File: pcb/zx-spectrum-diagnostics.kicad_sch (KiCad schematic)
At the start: 13 parts, among them J101 Conn_01x04, U101 Pico, U102 Pico

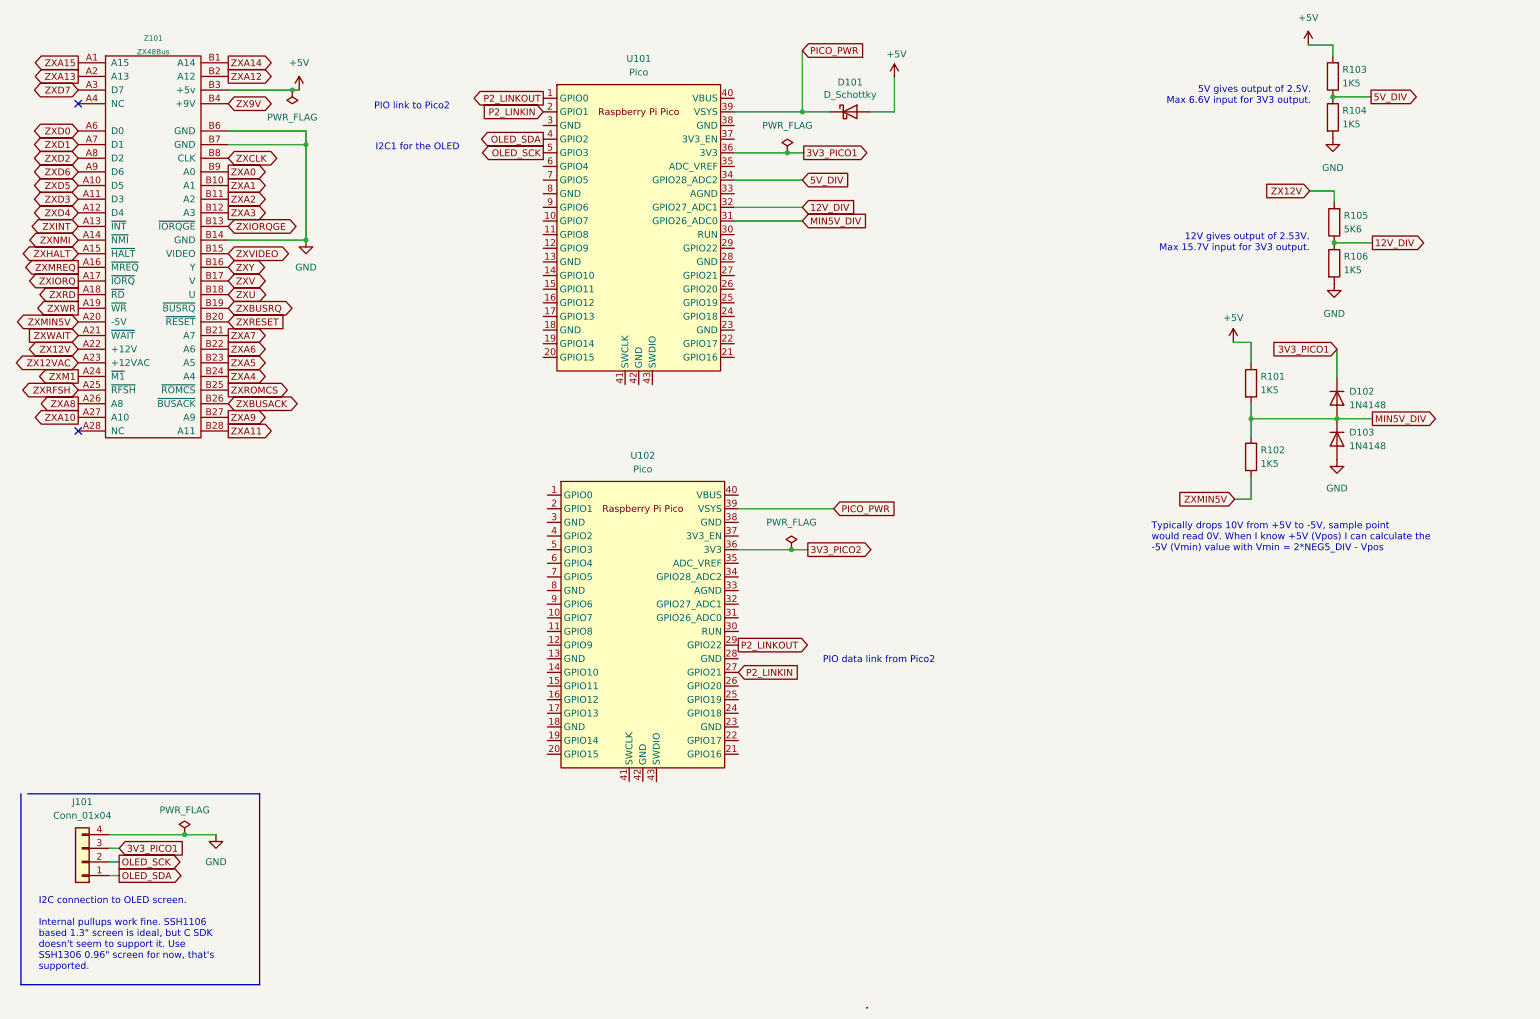
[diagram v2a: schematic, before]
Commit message: back out previous layout, rearrange connections to match edge connector
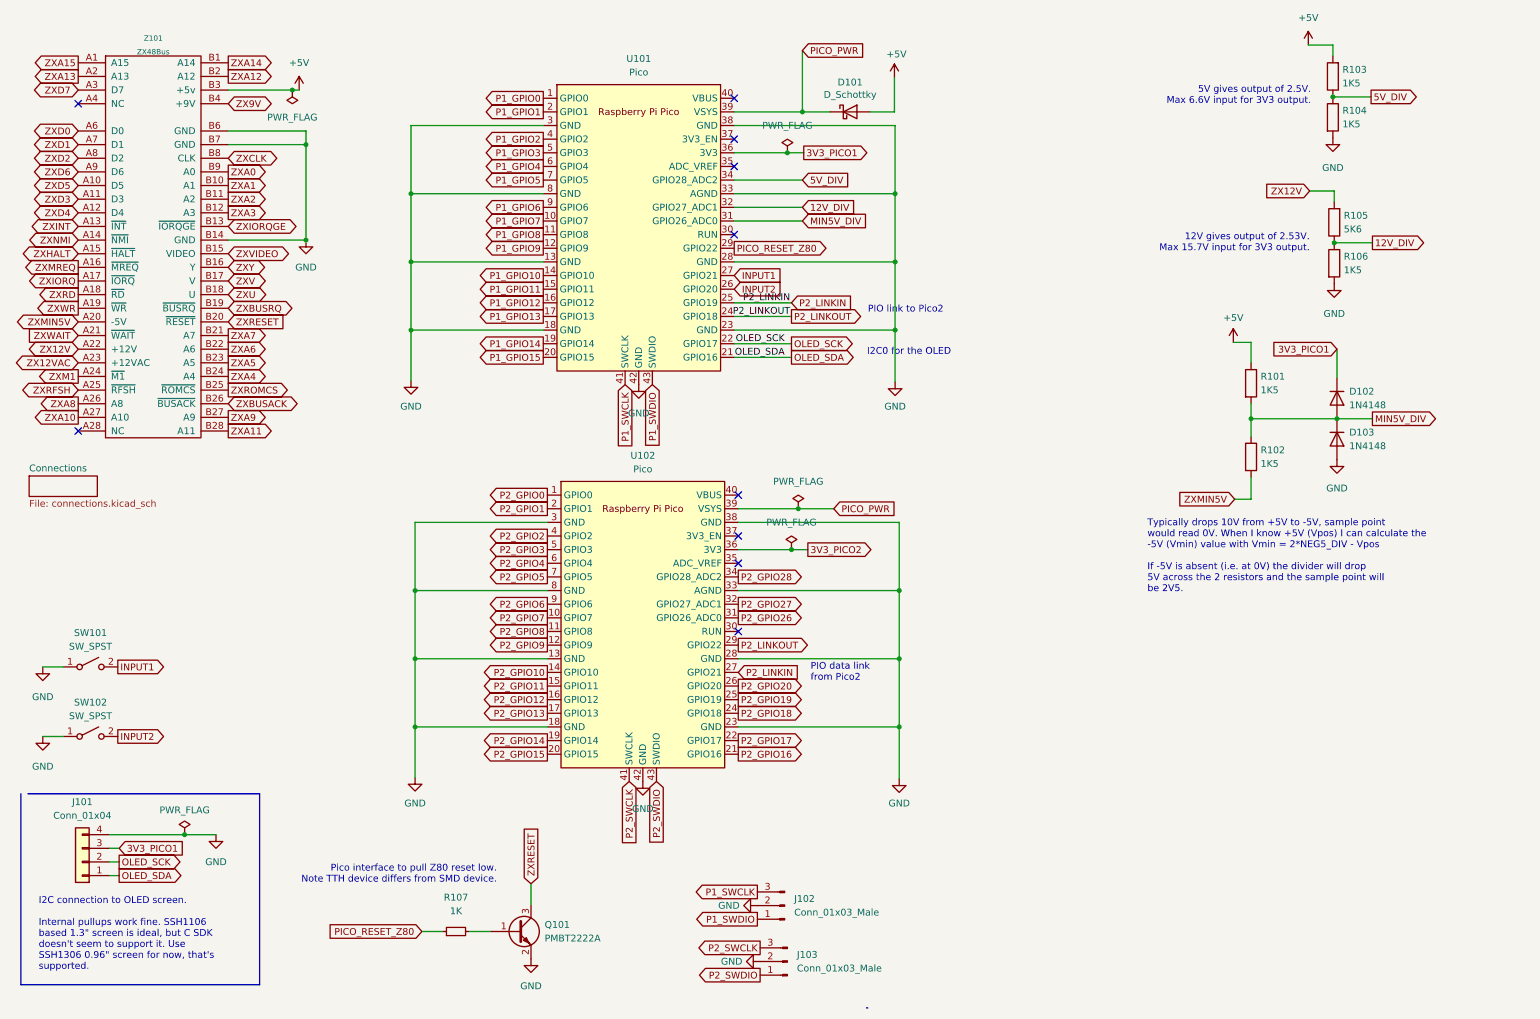
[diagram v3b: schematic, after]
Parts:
- added J102, J103: Conn_01x03_Male, Connector_PinSocket_2.54mm:PinSocket_1x03_P2.54mm_Vertical, symbol Connector:Conn_01x03_Male
- added Q101: PMBT2222A, Package_TO_SOT_SMD:TSOT-23_HandSoldering, symbol pmbt2222a:PMBT2222A
- added R107: 1K, Resistor_SMD:R_1206_3216Metric_Pad1.30x1.75mm_HandSolder, symbol Device:R_Small
- added SW101, SW102: SW_SPST, Button_Switch_THT:SW_PUSH_6mm_H4.3mm, symbol Switch:SW_SPST
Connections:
- net GND: now also U101.13 (GND), U101.18 (GND), U101.23 (GND), U101.28 (GND), U101.3 (GND), U101.33 (AGND), U101.38 (GND), U101.42 (GND), U101.8 (GND), U102.13 (GND), U102.18 (GND), U102.23 (GND), U102.28 (GND), U102.3 (GND), U102.33 (AGND), U102.38 (GND), U102.42 (GND), U102.8 (GND), J102.2 (Pin_2), J103.2 (Pin_2), Q101.2 (E), SW101.1 (A), SW102.1 (A)
- net OLED_SCK: now also U101.22 (GPIO17); no longer U101.5 (GPIO3)
- net OLED_SDA: now also U101.21 (GPIO16); no longer U101.4 (GPIO2)
- net P2_LINKIN: now also U101.25 (GPIO19); no longer U101.2 (GPIO1)
- net P2_LINKOUT: now also U101.24 (GPIO18); no longer U101.1 (GPIO0)
- net ZXRESET: now also Q101.3 (C)
- net P1_GPIO7: now reaches U101.10 (GPIO7)
- net P1_GPIO8: now reaches U101.11 (GPIO8)
- net P1_GPIO9: now reaches U101.12 (GPIO9)
- net P1_GPIO10: now reaches U101.14 (GPIO10)
- net P1_GPIO11: now reaches U101.15 (GPIO11)
- net P1_GPIO12: now reaches U101.16 (GPIO12)
- net P1_GPIO13: now reaches U101.17 (GPIO13)
- net P1_GPIO14: now reaches U101.19 (GPIO14)
- net P1_GPIO15: now reaches U101.20 (GPIO15)
- net INPUT2: now reaches U101.26 (GPIO20)
- net INPUT2: now also SW102.2 (B)
- net INPUT1: now reaches U101.27 (GPIO21)
- net INPUT1: now also SW101.2 (B)
- net PICO_RESET_Z80: now reaches U101.29 (GPIO22)
- net PICO_RESET_Z80: now also R107.1
- net P1_SWCLK: now reaches U101.41 (SWCLK)
- net P1_SWCLK: now also J102.3 (Pin_3)
- net P1_SWDIO: now reaches U101.43 (SWDIO)
- net P1_SWDIO: now also J102.1 (Pin_1)
- net P1_GPIO4: now reaches U101.6 (GPIO4)
- net P1_GPIO5: now reaches U101.7 (GPIO5)
- net P1_GPIO6: now reaches U101.9 (GPIO6)
- net P2_GPIO0: now reaches U102.1 (GPIO0)
- net P2_GPIO7: now reaches U102.10 (GPIO7)
- net P2_GPIO8: now reaches U102.11 (GPIO8)
- net P2_GPIO9: now reaches U102.12 (GPIO9)
- net P2_GPIO10: now reaches U102.14 (GPIO10)
- net P2_GPIO11: now reaches U102.15 (GPIO11)
- net P2_GPIO12: now reaches U102.16 (GPIO12)
- net P2_GPIO13: now reaches U102.17 (GPIO13)
- net P2_GPIO14: now reaches U102.19 (GPIO14)
- net P2_GPIO1: now reaches U102.2 (GPIO1)
- net P2_GPIO15: now reaches U102.20 (GPIO15)
- net P2_GPIO16: now reaches U102.21 (GPIO16)
- net P2_GPIO17: now reaches U102.22 (GPIO17)
- net P2_GPIO18: now reaches U102.24 (GPIO18)
- net P2_GPIO19: now reaches U102.25 (GPIO19)
- net P2_GPIO20: now reaches U102.26 (GPIO20)
- net P2_GPIO26: now reaches U102.31 (GPIO26_ADC0)
- net P2_GPIO27: now reaches U102.32 (GPIO27_ADC1)
- net P2_GPIO28: now reaches U102.34 (GPIO28_ADC2)
- net P2_GPIO2: now reaches U102.4 (GPIO2)
- net P2_SWCLK: now reaches U102.41 (SWCLK)
- net P2_SWCLK: now also J103.3 (Pin_3)
- net P2_SWDIO: now reaches U102.43 (SWDIO)
- net P2_SWDIO: now also J103.1 (Pin_1)
- net P2_GPIO3: now reaches U102.5 (GPIO3)
- net P2_GPIO4: now reaches U102.6 (GPIO4)
- net P2_GPIO5: now reaches U102.7 (GPIO5)
- net P2_GPIO6: now reaches U102.9 (GPIO6)
- new net: Q101.1 (B), R107.2
- new net P1_GPIO0: U101.1 (GPIO0)
- new net P1_GPIO1: U101.2 (GPIO1)
- new net P1_GPIO2: U101.4 (GPIO2)
- new net P1_GPIO3: U101.5 (GPIO3)
- no-connect marks 2 -> 10
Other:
- added sheet Connections (connections.kicad_sch)
- note added: "I2C0 for the OLED"
- note added: "Pico interface to pull Z80 reset low. Note TTH device differs from SMD device."
- note added: "Typically drops 10V from +5V to -5V, sample point would read 0V. When I know +5V (Vpos) I can calculate the -5V (Vmin) value with Vmin = 2*NEG5_DIV - Vpos If -5V is absent (i.e. at 0V) the divider will drop 5V across the 2 resistors and the sample point will be 2V5."
- note removed: "I2C1 for the OLED"
- note removed: "Typically drops 10V from +5V to -5V, sample point would read 0V. When I know +5V (Vpos) I can calculate the -5V (Vmin) value with Vmin = 2*NEG5_DIV - Vpos"

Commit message: v1.0 off to fab
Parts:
- D102, D103: footprint Diode_SMD:D_1206_3216Metric_Pad1.42x1.75mm_HandSolder -> Diode_SMD:D_SOD-123
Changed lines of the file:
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@@
       (effects (font (size 1.27 1.27)) (justify left))
     )
-    (property "Footprint" "Diode_SMD:D_1206_3216Metric_Pad1.42x1.75mm_HandSolder" (id 2) (at 259.842 92.456 0)
+    (property "Footprint" "Diode_SMD:D_SOD-123" (id 2) (at 259.842 92.456 0)
       (effects (font (size 1.27 1.27)) hide)
     )
@@
       (effects (font (size 1.27 1.27)) (justify left))
     )
-    (property "Footprint" "Diode_SMD:D_1206_3216Metric_Pad1.42x1.75mm_HandSolder" (id 2) (at 259.842 84.836 0)
+    (property "Footprint" "Diode_SMD:D_SOD-123" (id 2) (at 259.842 84.836 0)
       (effects (font (size 1.27 1.27)) hide)
     )
@@
     )
     (path "/d9d4c412-10f6-47b7-9c11-43e0dd422b75"
-      (reference "D102") (unit 1) (value "1N4148") (footprint "Diode_SMD:D_1206_3216Metric_Pad1.42x1.75mm_HandSolder")
+      (reference "D102") (unit 1) (value "1N4148") (footprint "Diode_SMD:D_SOD-123")
     )
     (path "/d3364c3f-7456-4539-86a5-d88591e950f5"
-      (reference "D103") (unit 1) (value "1N4148") (footprint "Diode_SMD:D_1206_3216Metric_Pad1.42x1.75mm_HandSolder")
+      (reference "D103") (unit 1) (value "1N4148") (footprint "Diode_SMD:D_SOD-123")
     )
     (path "/4306a88c-b446-420a-8a4d-c6b820db0ec2"

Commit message: change the layout to use the proper edge connector
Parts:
- Z101: footprint zxbus:ZX_Bus_Pin_Header -> zxedge:Spectrum_Edge_Connector
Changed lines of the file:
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@@
       (effects (font (size 0.9906 0.9906)))
     )
-    (property "Footprint" "zxbus:ZX_Bus_Pin_Header" (id 2) (at 30.48 103.632 0)
+    (property "Footprint" "zxedge:Spectrum_Edge_Connector" (id 2) (at 30.48 103.632 0)
       (effects (font (size 0.9906 0.9906)) hide)
     )
@@
     )
     (path "/28a893db-1c35-4c03-b308-f54ebb07c369"
-      (reference "Z101") (unit 1) (value "ZX48Bus") (footprint "zxbus:ZX_Bus_Pin_Header")
-    )
-  )
+      (reference "Z101") (unit 1) (value "ZX48Bus") (footprint "zxedge:Spectrum_Edge_Connector")
+    )
+  )

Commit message: schematic reworked, it's time to relayout the board. checkpoint here
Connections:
- net P1_GPIO0 is gone; now on net ZXD0: U101.1 (GPIO0)
- net P1_GPIO1 is gone; now on net ZXD1: U101.2 (GPIO1)
- net P1_GPIO10 is gone; now on net ZXMREQ: U101.14 (GPIO10)
- net P1_GPIO11 is gone; now on net ZXRD: U101.15 (GPIO11)
- net P1_GPIO12 is gone; now on net ZXWR: U101.16 (GPIO12)
- net P1_GPIO13 is gone; now on net ZXM1: U101.17 (GPIO13)
- net P1_GPIO14 is gone; now on net ZXCLK: U101.19 (GPIO14)
- net P1_GPIO15 is gone; now on net ZXINT: U101.20 (GPIO15)
- net P1_GPIO2 is gone; now on net ZXD2: U101.4 (GPIO2)
- net P1_GPIO3 is gone; now on net ZXD3: U101.5 (GPIO3)
- net P1_GPIO4 is gone; now on net ZXD4: U101.6 (GPIO4)
- net P1_GPIO5 is gone; now on net ZXD5: U101.7 (GPIO5)
- net P1_GPIO6 is gone; now on net ZXD6: U101.9 (GPIO6)
- net P1_GPIO7 is gone; now on net ZXD7: U101.10 (GPIO7)
- net P2_GPIO0 is gone; now on net ZXA0: U102.1 (GPIO0)
- net P2_GPIO1 is gone; now on net ZXA1: U102.2 (GPIO1)
- net P2_GPIO10 is gone; now on net ZXA10: U102.14 (GPIO10)
- net P2_GPIO11 is gone; now on net ZXA11: U102.15 (GPIO11)
- net P2_GPIO12 is gone; now on net ZXA12: U102.16 (GPIO12)
- net P2_GPIO13 is gone; now on net ZXA13: U102.17 (GPIO13)
- net P2_GPIO14 is gone; now on net ZXA14: U102.19 (GPIO14)
- net P2_GPIO15 is gone; now on net ZXA15: U102.20 (GPIO15)
- net P2_GPIO2 is gone; now on net ZXA2: U102.4 (GPIO2)
- net P2_GPIO20 is gone; now on net PICO_SIGNAL: U102.26 (GPIO20)
- net P2_GPIO3 is gone; now on net ZXA3: U102.5 (GPIO3)
- net P2_GPIO4 is gone; now on net ZXA4: U102.6 (GPIO4)
- net P2_GPIO5 is gone; now on net ZXA5: U102.7 (GPIO5)
- net P2_GPIO6 is gone; now on net ZXA6: U102.9 (GPIO6)
- net P2_GPIO7 is gone; now on net ZXA7: U102.10 (GPIO7)
- net P2_GPIO8 is gone; now on net ZXA8: U102.11 (GPIO8)
- net P2_GPIO9 is gone; now on net ZXA9: U102.12 (GPIO9)
- net P1_GPIO8 renamed PICO_SIGNAL
- net P1_GPIO9 renamed P1_BLIPPER
- net P2_GPIO19 renamed P2_BLIPPER
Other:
- note added: "I2C connection to OLED screen."
- note removed: "I2C connection to OLED screen. Internal pullups work fine. SSH1106 based 1.3" screen is ideal, but C SDK doesn't seem to support it. Use SSH1306 0.96" screen for now, that's supported."
- moved on the sheet: J101
